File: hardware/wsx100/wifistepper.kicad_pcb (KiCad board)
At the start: 4 copper layers, 77.6 x 57.3 mm, 91 parts, among them J1 Barrel_Jack_Switch, J2 Screw_Terminal, J3 Conn_01x10, J4 Conn_01x10, J5 Conn_01x02, SW1 SW_SPST, U1 ESP-WROOM-02, U2 powerSTEP01, U3 MAX15062A, U4 ATECC508A

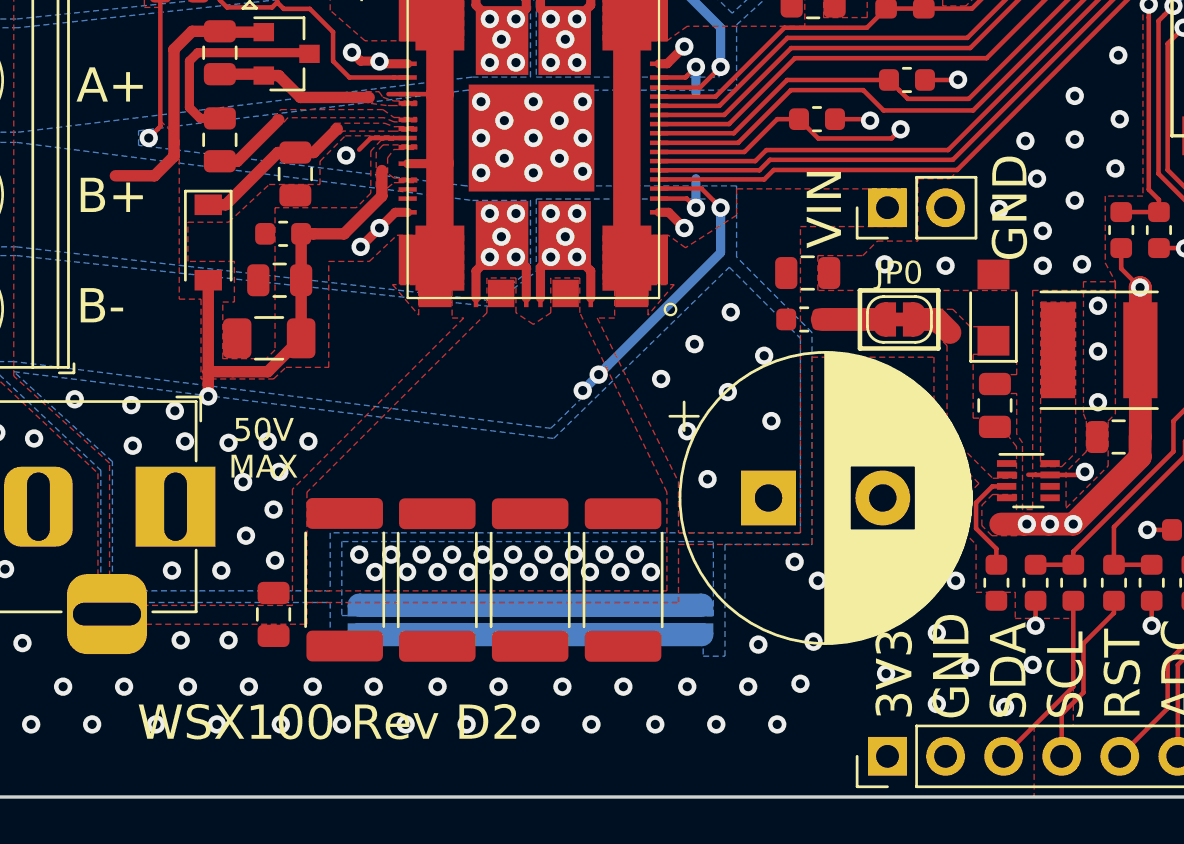
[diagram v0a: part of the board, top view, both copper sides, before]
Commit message: Board design update with more firmware features
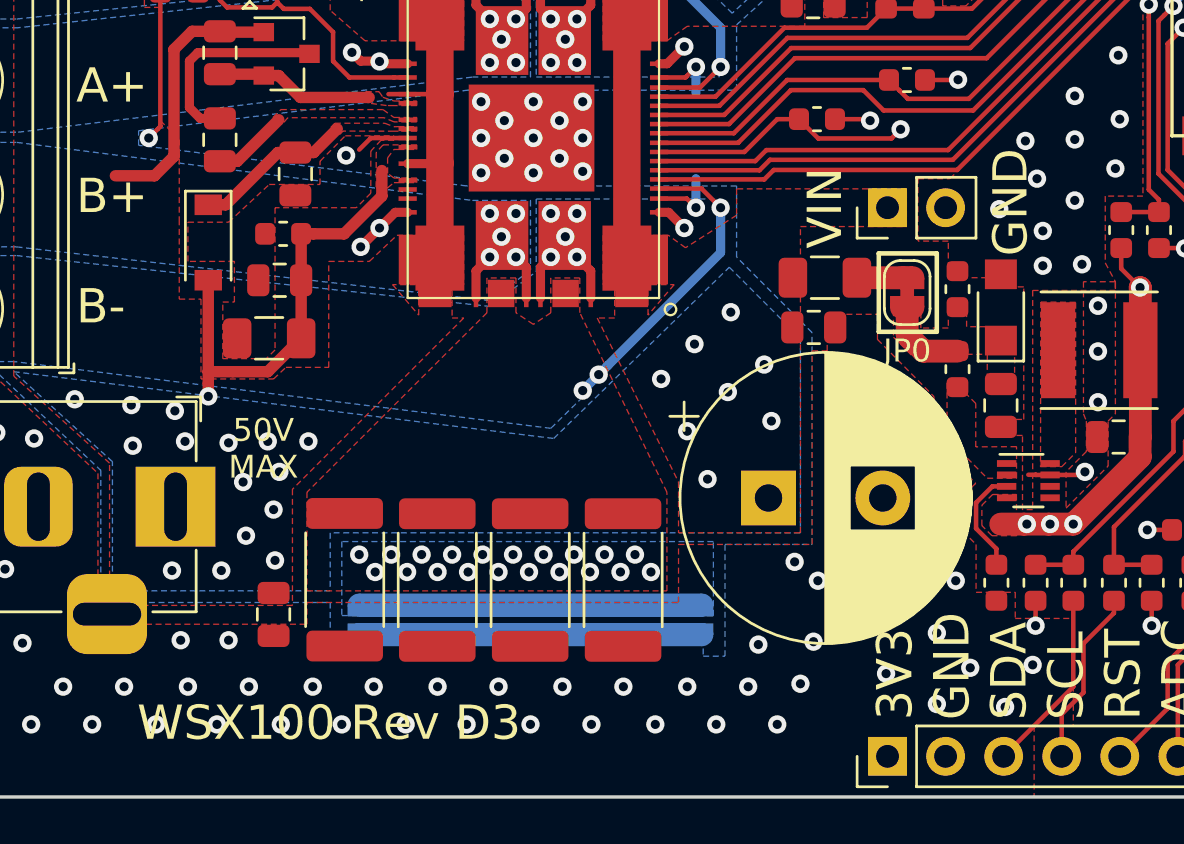
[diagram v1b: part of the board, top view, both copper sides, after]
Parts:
- removed FB1: Ferrite_Bead_Small, Inductor_SMD:L_0603_1608Metric
- removed the REF** at (46.6, 66.3)
- added R30: 10, Resistor_SMD:R_1206_3216Metric, F.Cu at (76.0, 95.9)
- added R31: 47K, Resistor_SMD:R_0603_1608Metric, F.Cu at (81.8, 96.4)
- added R32: 000, Resistor_SMD:R_0603_1608Metric, F.Cu at (81.8, 99.9)
- moved C6 2.40 mm to (75.5, 98.1)
- moved JP0 1.22 mm to (79.6, 96.5), turned to 270 degrees
- moved D7 0.32 mm to (83.7, 97.2)
- moved C18 0.26 mm to (83.7, 101.5), turned to 270 degrees
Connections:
- J1 pad 3: (no net) -> Net-(J1-Pad3)
- U2 pad 63: (no net) -> Net-(U2-Pad63)
- U2 pad 64: (no net) -> Net-(U2-Pad64)
- U3 pad 1: Net-(C18-Pad1) -> Net-(R32-Pad1)
- U3 pad 2: Net-(C18-Pad1) -> Net-(R32-Pad1)
- U3 pad 5: (no net) -> Net-(U3-Pad5)
- U3 pad 6: (no net) -> Net-(U3-Pad6)
- U4 pad 1: (no net) -> Net-(U4-Pad1)
- U4 pad 2: (no net) -> Net-(U4-Pad2)
- U4 pad 3: (no net) -> Net-(U4-Pad3)
- U4 pad 7: (no net) -> Net-(U4-Pad7)
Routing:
- net Net-(C18-Pad1): track 1.79 -> 3.40 mm
- net Net-(JP0-Pad1): track 2.73 -> 2.20 mm
- net GND: vias 189 -> 187
- added copper zone on F.Cu, net Net-(R32-Pad1)
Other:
- board text added: "Good Robotics (2020)"
- board text added: "WSX100 Rev D3"
- board text removed: "Good Robotics (2019)"
- board text removed: "WSX100 Rev D2"
